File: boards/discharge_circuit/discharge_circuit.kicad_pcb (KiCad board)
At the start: 2 copper layers, 99.1 x 48.3 mm, 14 parts, among them J1 Unfused TS, J2 Shutdown Circuit, J3 TSMP, J4 TSAL, J5 IMD, J6 EM/Precharge, K1 G2RL-1-E

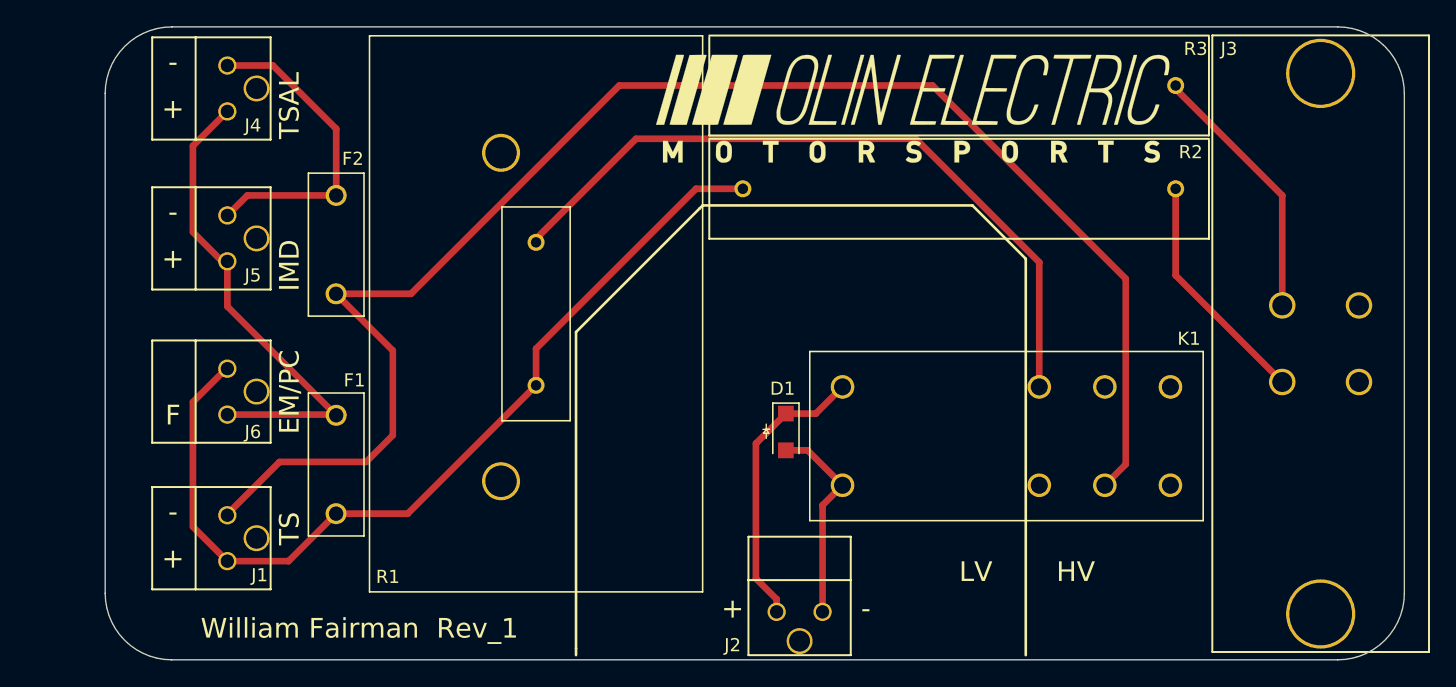
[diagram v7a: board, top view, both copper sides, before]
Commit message: made revisions to discharge circuit
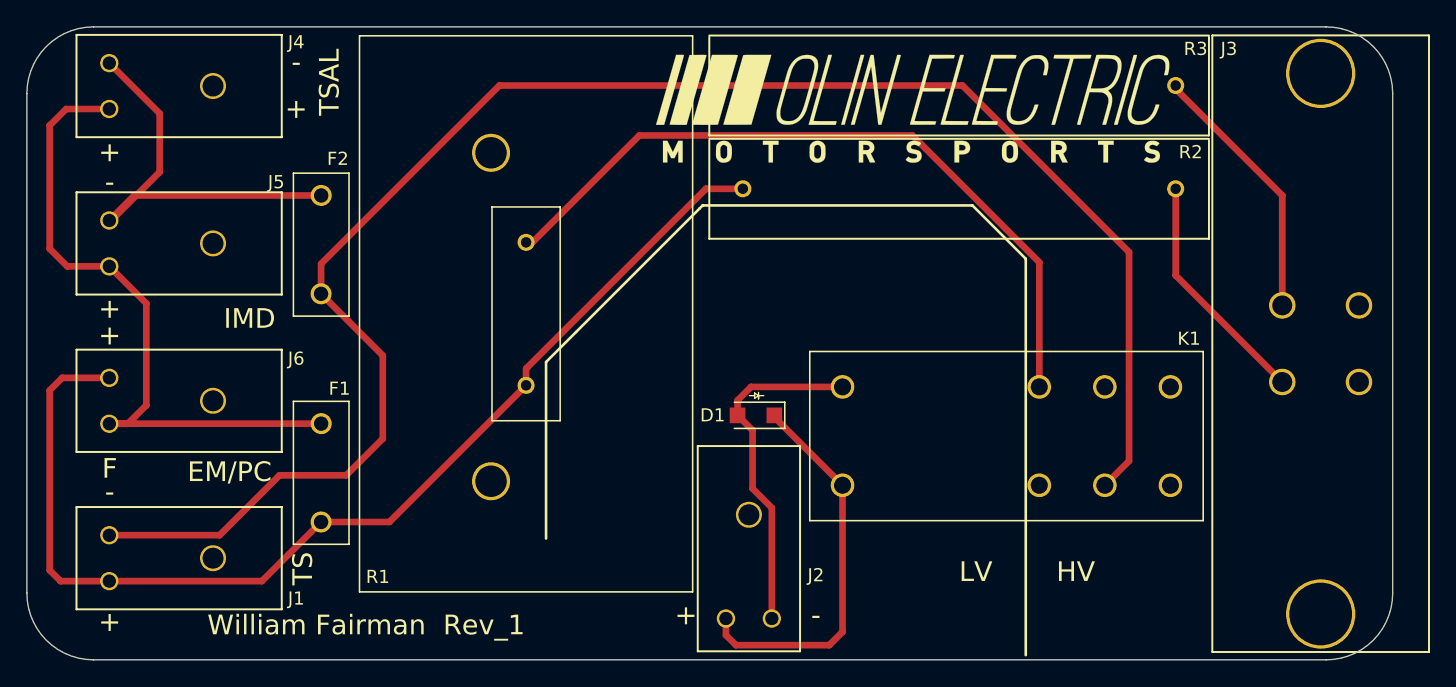
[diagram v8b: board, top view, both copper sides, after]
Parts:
- J1, J2, J4, J5, J6: footprint footprints:Ultrafit_2 -> footprints:Ultrafit_2_RA
- moved J1 9.13 mm to (97.0, 67.6)
- moved J6 9.03 mm to (97.0, 55.6)
- moved J5 9.01 mm to (97.0, 43.6)
- moved J4 9.00 mm to (97.0, 31.6)
- moved J2 7.38 mm to (144.0, 73.9), turned to 90 degrees
- moved D1 2.62 mm to (146.3, 58.4), turned to 180 degrees
- moved F1 1.31 mm to (113.2, 59.1)
- moved F2 1.14 mm to (113.2, 41.7)
- moved R1 0.76 mm to (128.8, 56.1)
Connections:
- D1 pad 1: /Shutdown -> GND
- D1 pad 2: GND -> /Shutdown
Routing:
- net /TS+Unfused: track 69.6 -> 85.4 mm
- net /TS+Fused: track 37.4 -> 51.6 mm
- net GND: track 15.7 -> 29.6 mm
- net /TS-Unfused: track 117.4 -> 130.2 mm
- net /TS-Fused: track 24.3 -> 32.2 mm
- net /Shutdown: track 21.9 -> 26.1 mm
- net Net-(K1-Pad2): track 55.4 -> 56.0 mm
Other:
- board size 99.1 x 48.3 mm -> 104.1 x 48.3 mm
- net class Default: via_dia 0.6 -> 0.6096; via_drill 0.4 -> 0.3048
- rule via_min_size: 0.381 -> 0.6096
